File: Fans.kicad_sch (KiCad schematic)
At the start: 10 parts, among them J401 Fan Connector, J402 Fan Voltage Selection, J403 Fan Connector, J404 Fan Voltage Selection, J405 Fan Connector, J406 Fan Voltage Selection, J407 Fan Connector, J408 Fan Voltage Selection, Q401 Si4532DY, Q402 Si4532DY

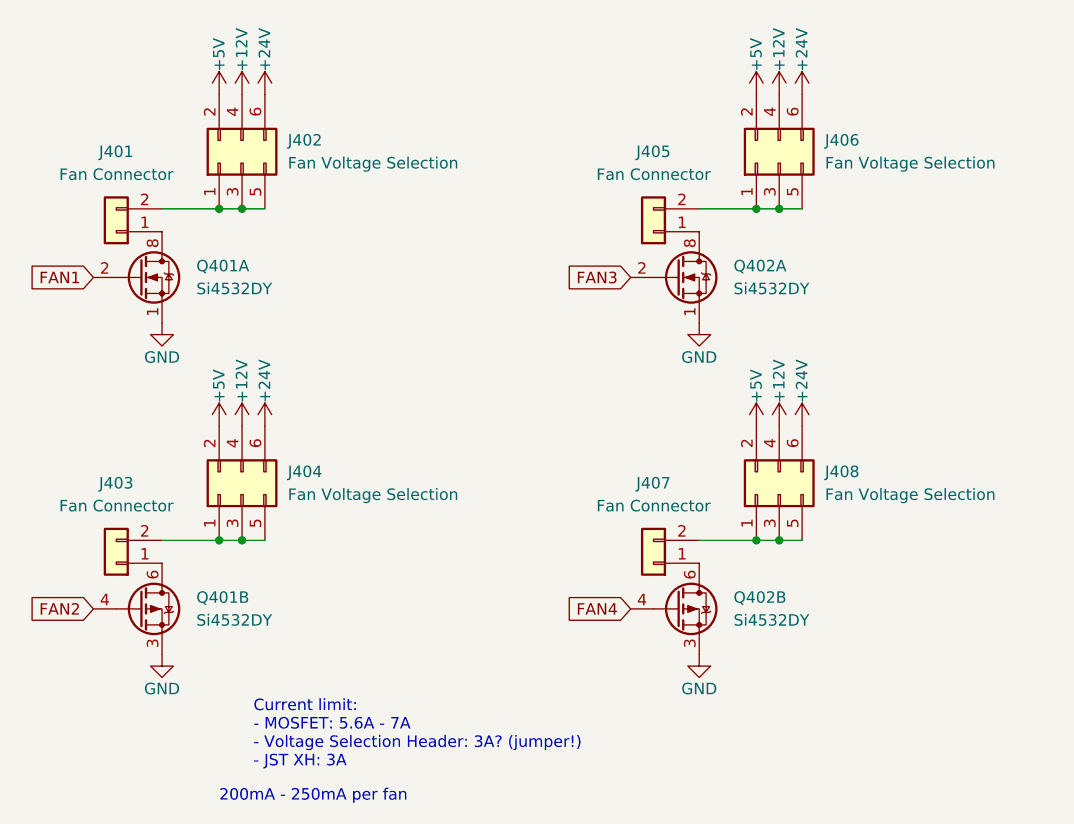
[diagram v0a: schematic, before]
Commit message: Assigning a lot of values to components Change MOSFETS for different (correct) ones Copy Motor1 to Motor2-4 Guess max current per voltage on PowerSupply schema
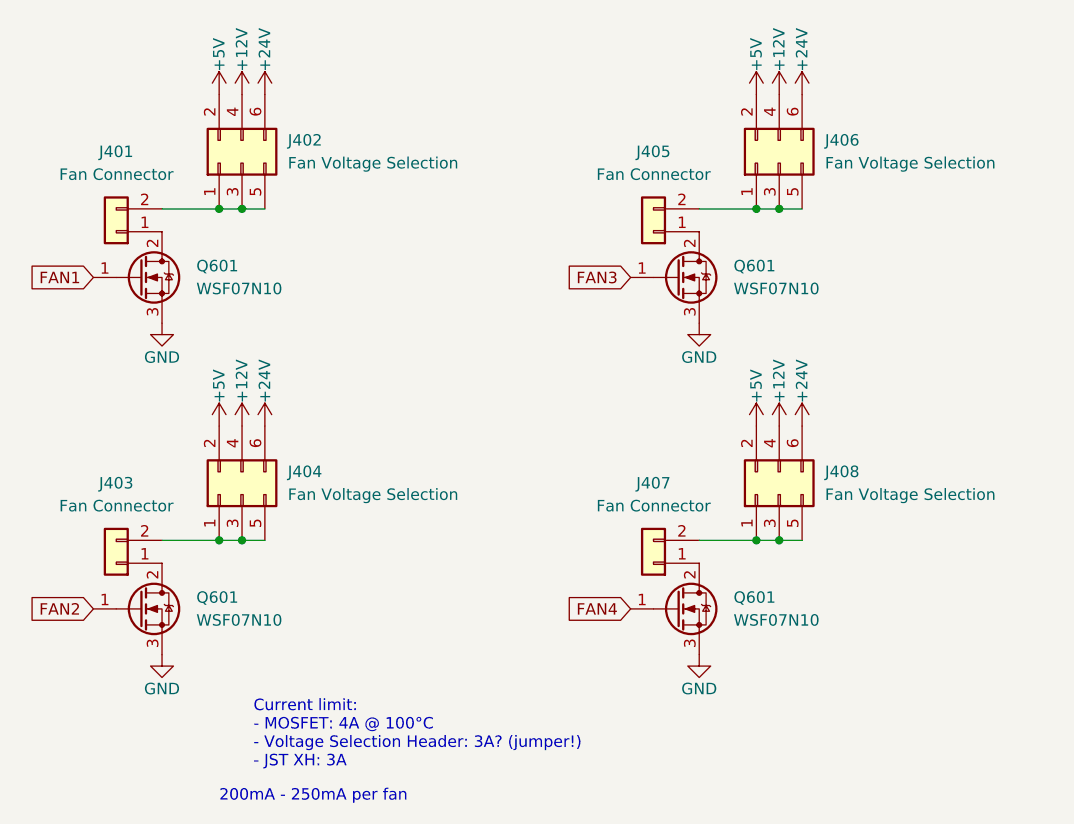
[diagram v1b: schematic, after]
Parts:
- removed Q401, Q402: Si4532DY, Package_SO:SOIC-8_3.9x4.9mm_P1.27mm, symbol Transistor_FET:Si4532DY
- added Q601 (x4): WSF07N10, Package_TO_SOT_SMD:TO-252-2, symbol Transistor_FET:QM6006D
- J401, J403, J405, J407: LCSC (none) -> C265283
- J402, J404, J406, J408: LCSC (none) -> -; Mouser (none) -> -
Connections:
- net FAN1: now also Q601.1 (G)
- net FAN2: now also Q601.1 (G)
- net FAN3: now also Q601.1 (G)
- net FAN4: now also Q601.1 (G)
- net GND: now also Q601.3 (S), Q601.3 (S), Q601.3 (S), Q601.3 (S)
- net at J405.1 (Pin_1): now also Q601.2 (D)
- net at J403.1 (Pin_1): now also Q601.2 (D)
- net at J401.1 (Pin_1): now also Q601.2 (D)
- net at J407.1 (Pin_1): now also Q601.2 (D)
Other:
- note added: "Current limit: - MOSFET: 4A @ 100°C - Voltage Selection Header: 3A? (jumper!) - JST XH: 3A"
- note removed: "Current limit: - MOSFET: 5.6A - 7A - Voltage Selection Header: 3A? (jumper!) - JST XH: 3A"

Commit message: Complete schematics Assign every value (very few exceptions) Change TCM5160 from on-board to separate module Add fuses Add power supplies (LDO + 2x buck converter)
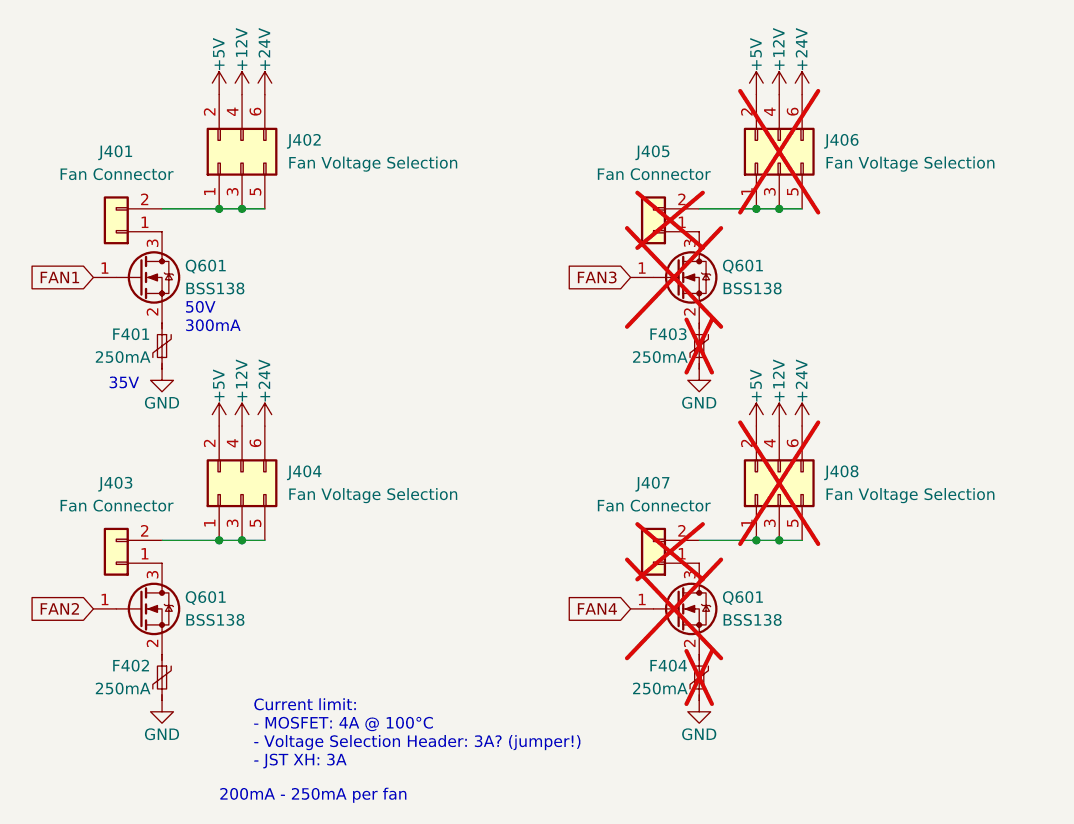
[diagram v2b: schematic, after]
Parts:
- removed Q601 (x3): WSF07N10, Package_TO_SOT_SMD:TO-252-2, symbol Transistor_FET:QM6006D
- added F401, F402, F403, F404: 250mA, Resistor_SMD:R_0603_1608Metric, symbol Device:Polyfuse_Small
- added Q601 (x3): BSS138, Package_TO_SOT_SMD:SOT-23, symbol Transistor_FET:BSS138
- J405, J406, J407, J408: now not fitted
- Q601: value WSF07N10 -> BSS138; footprint Package_TO_SOT_SMD:TO-252-2 -> Package_TO_SOT_SMD:SOT-23; symbol Transistor_FET:QM6006D -> Transistor_FET:BSS138; LCSC C719117 -> C400505
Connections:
- net FAN2: now also Q601.1 (G)
- net FAN3: now also Q601.1 (G)
- net FAN4: now also Q601.1 (G)
- net GND: now also F401.2, F402.2, F403.2, F404.2; no longer Q601.3 (S)
- net at J405.1 (Pin_1): now also Q601.3 (D)
- net at J403.1 (Pin_1): now also Q601.3 (D)
- net at Q601.2 (S): now also F401.1; no longer J401.1 (Pin_1)
- net at J407.1 (Pin_1): now also Q601.3 (D)
- new net: F403.1, Q601.2 (S)
- new net: F402.1, Q601.2 (S)
- new net: F404.1, Q601.2 (S)
- new net: J401.1 (Pin_1), Q601.3 (D)
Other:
- note added: "35V"
- note added: "50V 300mA"

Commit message: Finish wiring PCB
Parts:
- F403, F404, J405, J406, J407, J408, Q601: now fitted
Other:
- note added: "Only 1 jumper!"
